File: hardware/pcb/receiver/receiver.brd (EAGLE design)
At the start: 100 x 100 mm, 79 parts, among them X1 5-1634506-1H

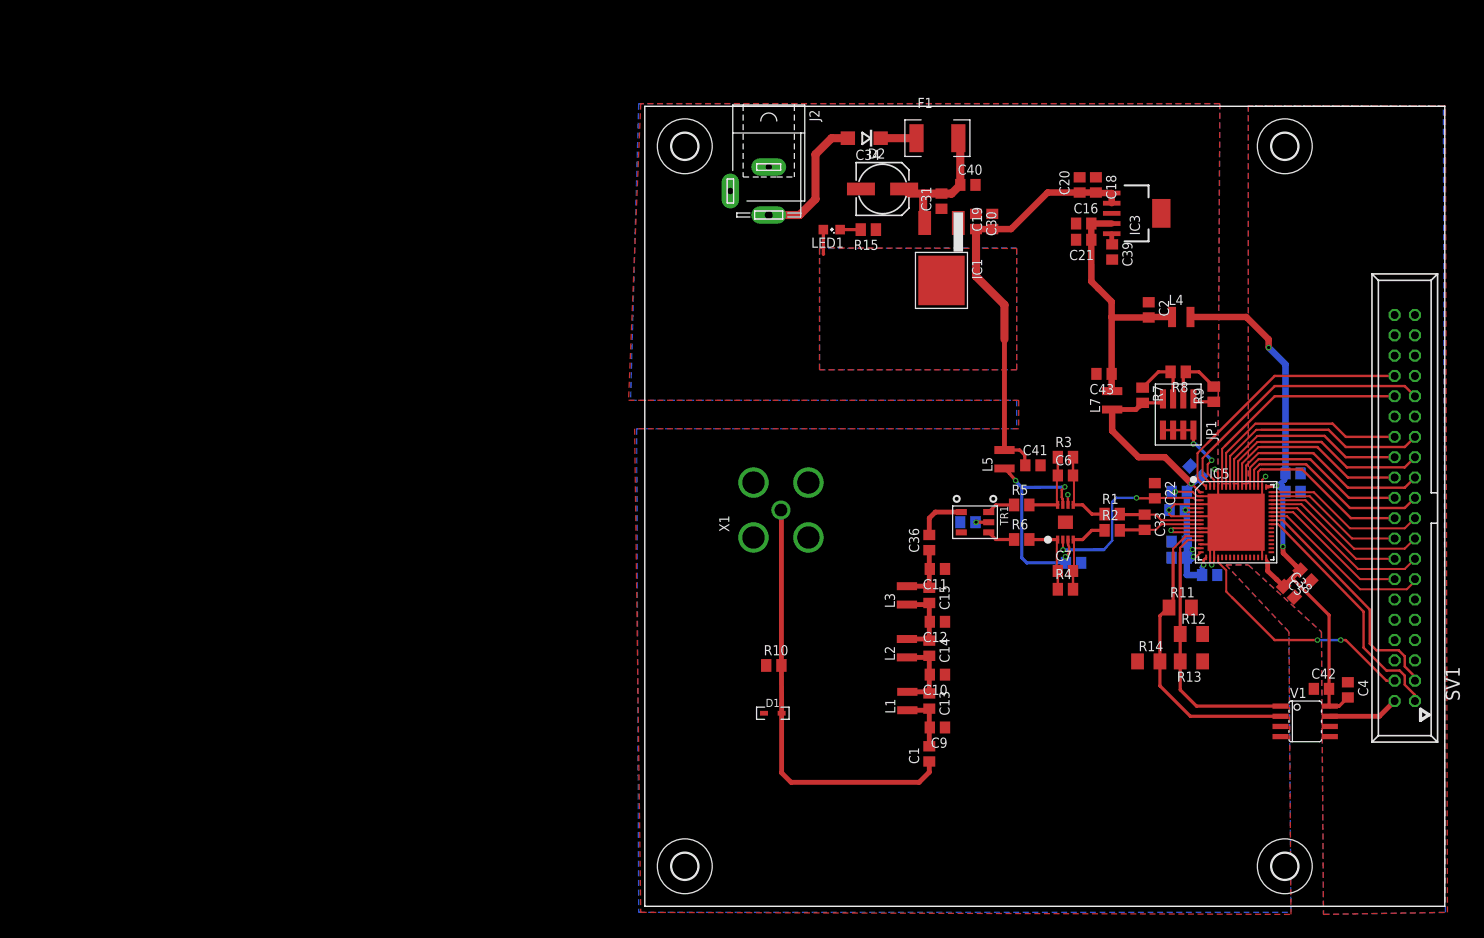
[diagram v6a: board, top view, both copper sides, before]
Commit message: hw: added optional mta100
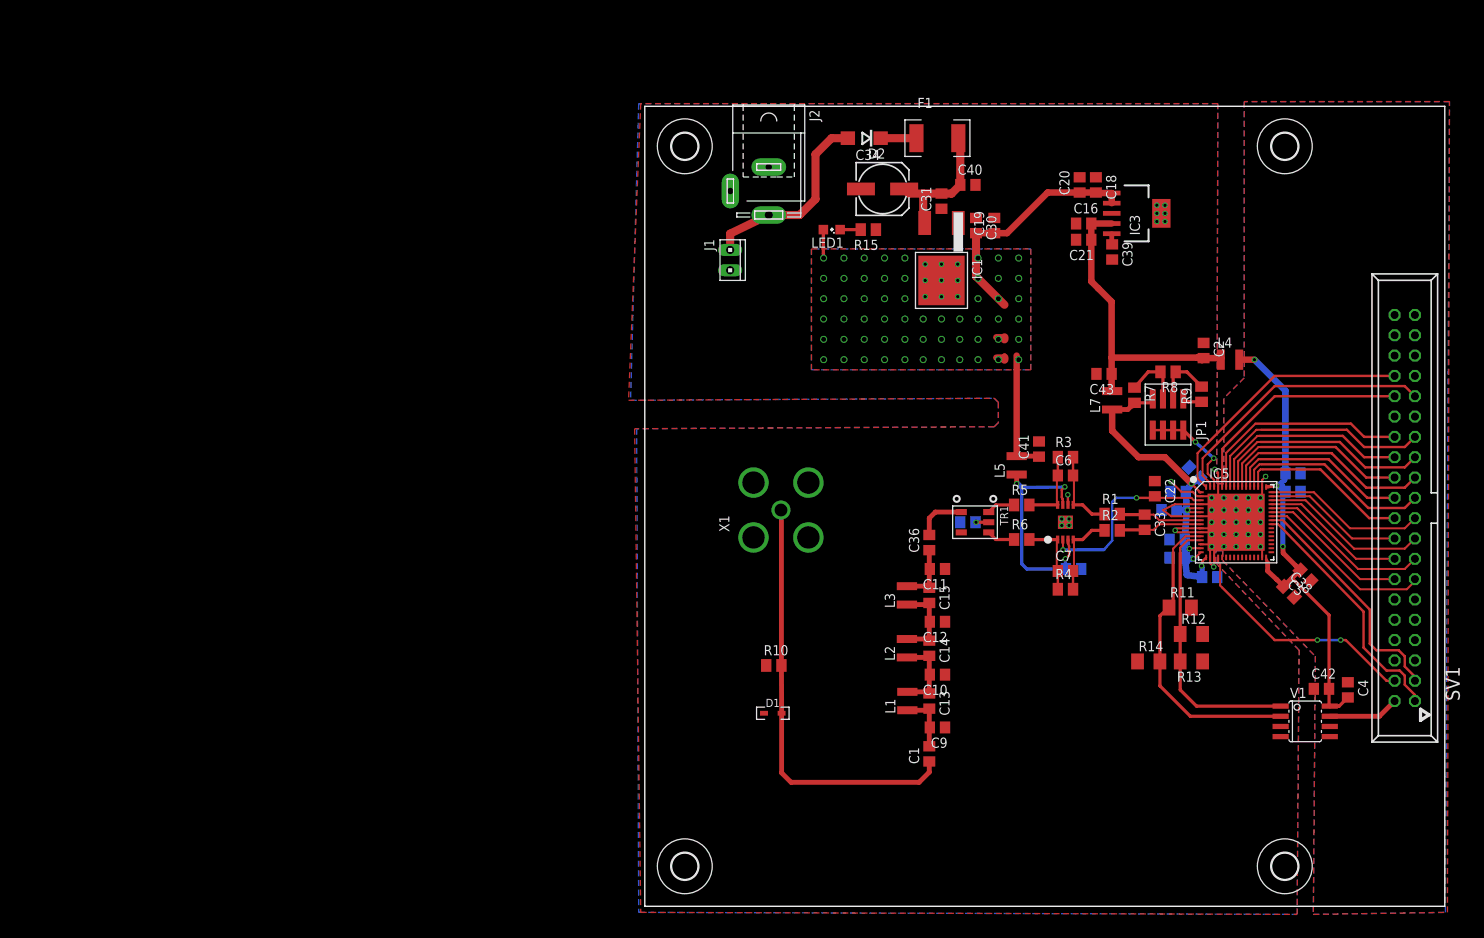
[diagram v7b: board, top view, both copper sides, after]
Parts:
- added J1: (no value), con-amp:10X02MTA
- moved C2 8.53 mm to (69.8, 69.5)
- moved L4 8.10 mm to (73.2, 68.3)
- moved C41 2.17 mm to (49.3, 57.1), turned to 90 degrees
- moved L5 1.70 mm to (46.5, 55.1)
- moved R9 1.52 mm to (69.6, 64.0)
- moved JP1 1.27 mm to (67.3, 61.5)
- moved R8 1.27 mm to (65.4, 66.8)
- moved C24 1.02 mm to (65.5, 49.5)
- moved R7 1.02 mm to (61.2, 63.9)
- moved C8 0.76 mm to (53.6, 42.2)
- moved C19 0.57 mm to (43.7, 85.1)
- moved C30 0.51 mm to (41.4, 85.1)
- moved C29 0.36 mm to (66.5, 45.8)
- moved C22 0.25 mm to (63.8, 52.2)
- moved C26 0.25 mm to (66.5, 43.6)
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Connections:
- net 12-18V: now also J1.2
- net GND: now also J1.1
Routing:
- net VDD: track 73.5 -> 62.7 mm
- net 12-18V: track 17.2 -> 24.5 mm
- net +3V3: track 32.2 -> 38.7 mm
- net +5V: track 56.9 -> 52.1 mm, vias 0 -> 66
- net +3V3A_ADC: track 49.9 -> 51.1 mm
- net MODE: track 12.6 -> 13.2 mm
- net +5V_AMP: track 28.8 -> 29.4 mm
- net GND: track 80.2 -> 80.6 mm, vias 7 -> 41

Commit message: hw: gnd vias
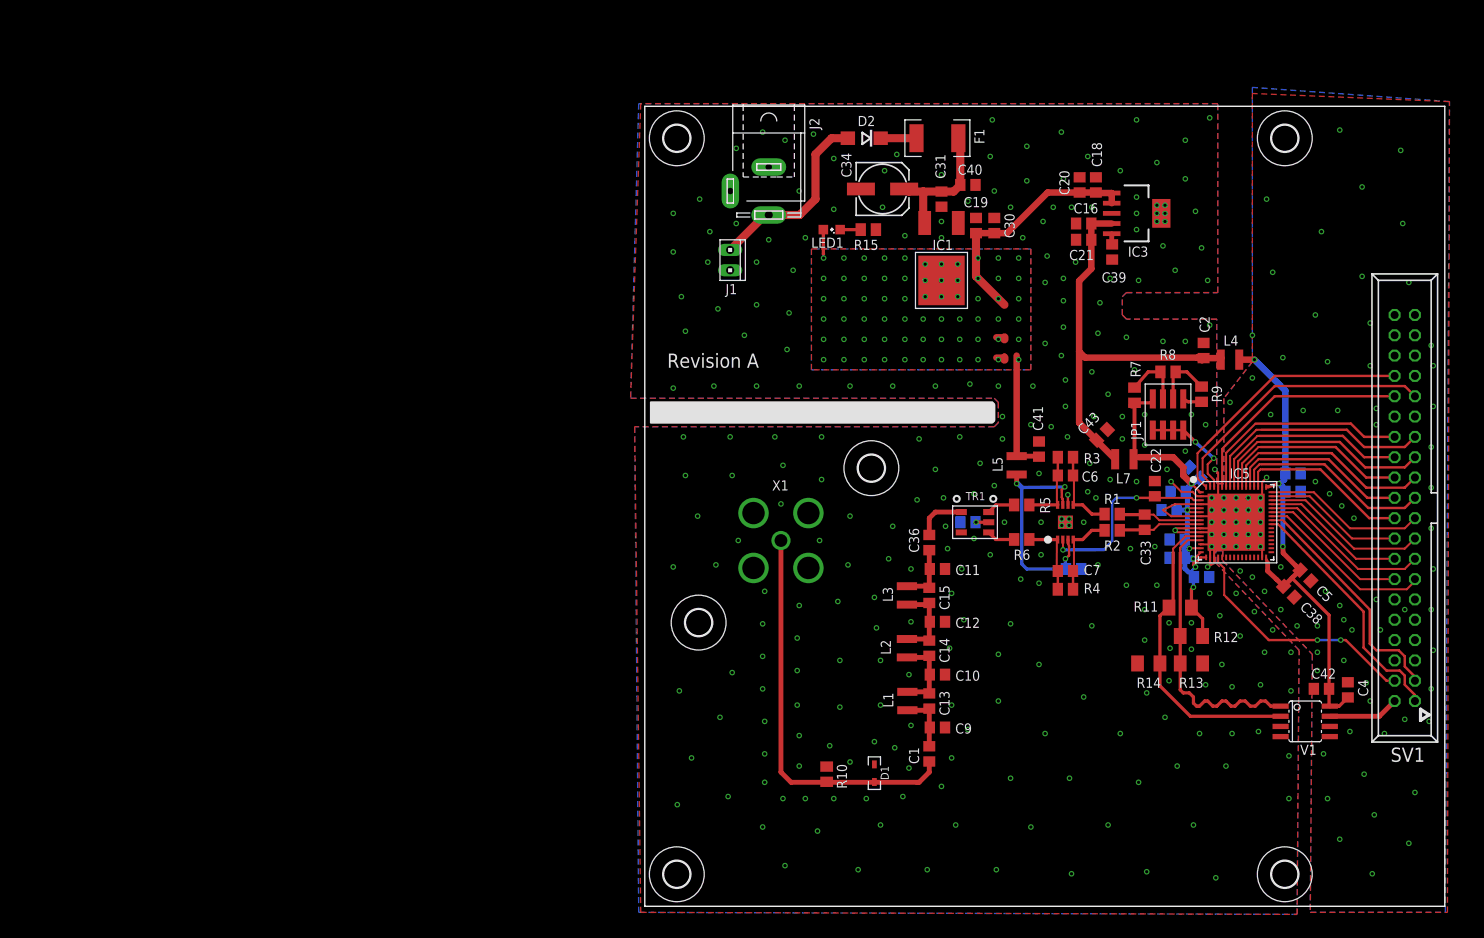
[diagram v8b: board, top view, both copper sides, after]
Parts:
- added H5, H6: MOUNT-HOLE3.3, holes:3,3
- moved R10 15.1 mm to (22.7, 16.5), turned to 270 degrees
- moved D1 14.7 mm to (28.7, 16.6), turned to 270 degrees
- moved C43 7.62 mm to (57.1, 58.9), turned to 45 degrees
- moved L7 7.52 mm to (59.9, 55.9), turned to 180 degrees
- moved X1 3.81 mm to (17.0, 45.7)
- moved H1 1.41 mm to (4.00, 4.00)
- moved H2 1.41 mm to (4.00, 96.0)
- moved C28 1.02 mm to (69.6, 41.1)
- moved H3 1.00 mm to (80.0, 96.0)
- moved H4 1.00 mm to (80.0, 4.00)
- moved R12 0.25 mm to (68.3, 33.8)
- moved R13 0.25 mm to (68.3, 30.4)
- moved R14 0.25 mm to (63.0, 30.4)
- moved C31 0.25 mm to (37.1, 88.4)
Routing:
- net +3V3: track 38.7 -> 53.0 mm
- net +3V3A_ADC: track 51.1 -> 57.2 mm, vias 5 -> 6
- net ENC_P: track 34.1 -> 36.7 mm
- net N$2: track 53.7 -> 55.9 mm
- net 12-18V: track 24.5 -> 23.8 mm
- net GND: track 80.6 -> 80.9 mm, vias 41 -> 362
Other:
- board text added: "Revision A"
